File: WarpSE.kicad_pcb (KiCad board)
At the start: 4 copper layers, 112.1 x 102.1 mm, 137 parts, among them J1 MacSEPDS, J2 JTAG, J3 microUSB, J4 DBG, Q1 MMBT3904, Q2 DNP, U1 XC95144XL-TQ100, U10 39SF040, U11 39SF040, U12 CH340G, U13 74AHCT573PW, U14 MC68HC000FN20, U15 74AHCT573PW, U16 74AHCT573PW, U17 74AHCT573PW, U18 74AHCT573PW, U19 74AHCT573PW, U2 74AHCT573PW, U20 74AHCT573PW, U21 74AHCT573PW, U22 74AHCT573PW, U23 74AHCT573PW, U24 74AHCT573PW, U25 LM66100DCK, U26 74LVC1G34GW, U27 74LVC1G34GW, U28 74LVC1G34GW, U29 74LVC1G34GW, U3 AZ1117CH-3.3TRG1, U4 LM66100DCK, U5 50M, U6 74LVC1G74DC, U7 74LVC1G74DC, U8 KM48C2100, U9 KM48C2100, Y1 12M

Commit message: Board changes
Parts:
- removed REF**: PLCC-32_SMDSocket, stdpads:PLCC-32_SMDSocket
- added R38: 1k, stdpads:R_0603, F.Cu at (149.4, 68.7)
- added R39: 1k, stdpads:R_0603, F.Cu at (147.8, 68.7)
- J4: footprint stdpads:PinSocket_2x06_P2.54mm_Vertical -> stdpads:PinSocket_2x06_P2.00mm_Vertical
- U5: value 50M -> SiT2001; footprint stdpads:Crystal_SMD_3225-4Pin_3.2x2.5mm -> stdpads:SOT-23-5
- moved C53 4.41 mm to (125.6, 87.4), turned to -90 degrees
- moved J4 3.33 mm to (105.1, 116.6)
- moved C22 3.28 mm to (103.8, 114.4)
- moved R5 2.06 mm to (132.4, 90.7), turned to 90 degrees
- moved U5 1.65 mm to (128.6, 87.6), turned to 90 degrees
- moved R3 1.15 mm to (127.6, 90.1)
- moved C11 0.85 mm to (122.5, 59.0)
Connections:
- J1 pad C5: /Control/Mac~{BG} -> /PDS/~{BG}
- U1 pad 63: /Control/RA11 -> /Control/BA19
- U1 pad 73: /Control/Mac~{BG} -> /Control/BA18
- U10 pad 28: /Control/RA8 -> /Control/BA18
- U10 pad 29: /Control/RA11 -> /Control/BA19
- U11 pad 25: /Control/RA11 -> /Control/BA19
- U11 pad 26: /Control/RA8 -> /Control/BA18
- U5 pad 1: CLKEN -> GND
- U5 pad 2: GND -> unconnected-(U5-NC-Pad2)
- U5 pad 3: Net-(U5-Output) -> CLKEN
- U8 pad 8: /Control/RA11 -> unconnected-(U8-A11/NC-Pad8)
- U9 pad 10: /Control/RA1 -> /Control/RA2
- U9 pad 11: /Control/RA0 -> /Control/RA1
- U9 pad 12: /Control/RA10 -> /Control/RA0
- U9 pad 13: /Control/RA11 -> /Control/RA3
- U9 pad 8: /Control/RA3 -> unconnected-(U9-A11/NC-Pad8)
- U9 pad 9: /Control/RA2 -> /Control/RA10
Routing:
- net /Control/BA19: track 0.00 -> 173.6 mm, vias 0 -> 6
- net /Control/RA11: track 169.8 -> 0.00 mm, vias 6 -> 0
- net /Control/BA18: track 0.00 -> 153.7 mm, vias 0 -> 7
- net /Control/Mac~{BG}: track 103.4 -> 0.00 mm, vias 3 -> 0
- net /Control/RA8: track 153.2 -> 109.9 mm, vias 6 -> 2
- net /Control/RA3: track 115.6 -> 121.8 mm
- net /Control/DBG1_RAMWS: track 34.7 -> 40.1 mm, vias 1 -> 2
- net /Control/RA10: track 111.2 -> 115.8 mm
- net /Control/CLKINu: track 11.3 -> 14.4 mm
- net /Control/DBG0_ROMWS: track 36.3 -> 38.8 mm, vias 2 -> 1
- net +3V3: track 562.9 -> 565.1 mm, vias 93 -> 92
- net /Buf/GA20: track 107.5 -> 105.4 mm, vias 6 -> 5
- net /Buf/GA21: track 93.2 -> 94.5 mm, vias 5 -> 4
- net CLKEN: track 159.0 -> 158.1 mm
- net Net-(U6-CK): track 8.03 -> 8.90 mm
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
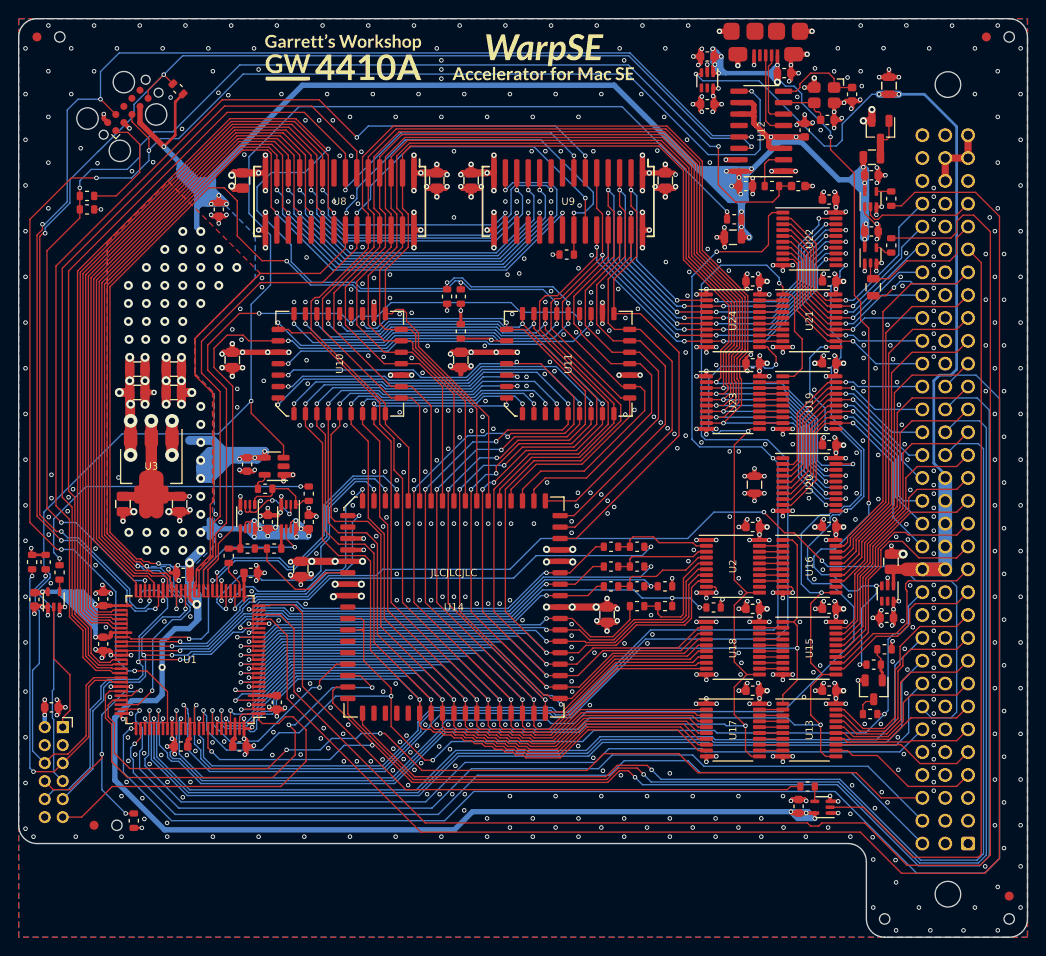
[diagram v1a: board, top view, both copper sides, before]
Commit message: Before remove first clock input buffer
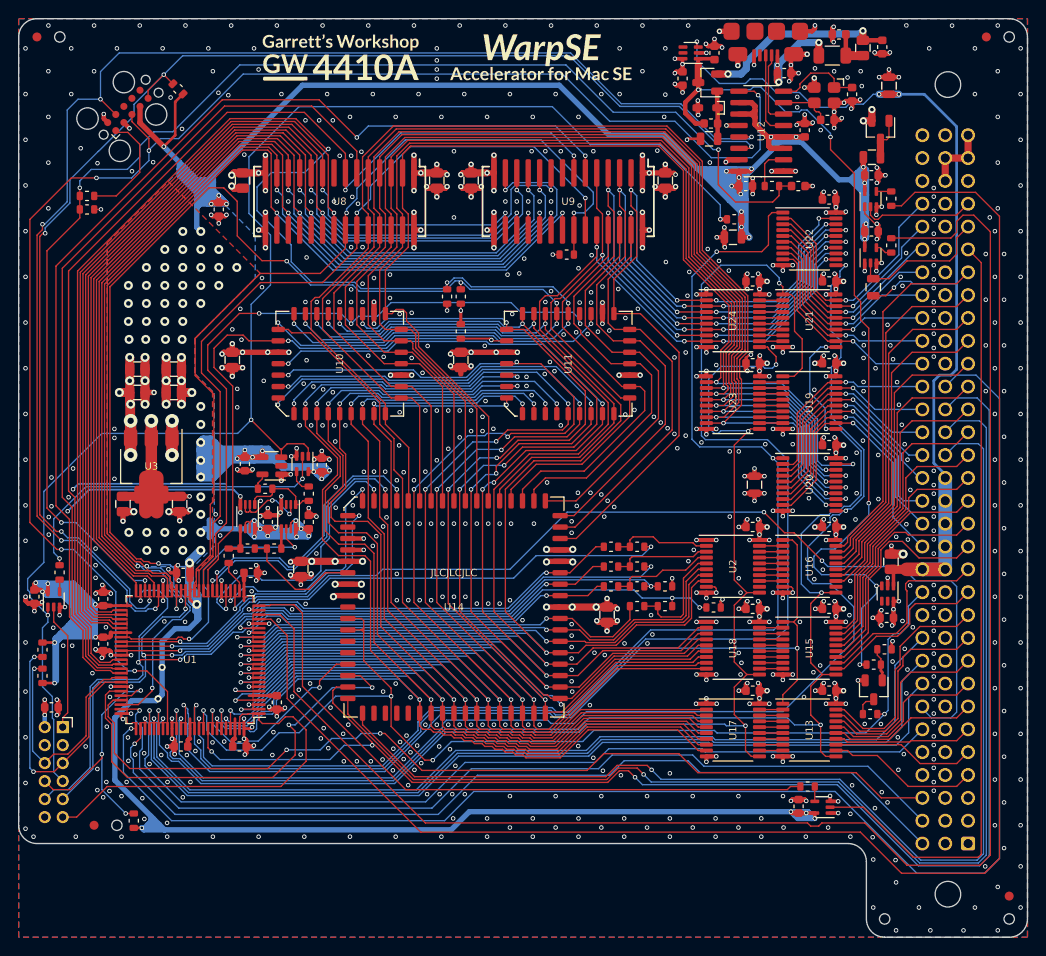
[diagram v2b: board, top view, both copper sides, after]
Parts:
- added C24: 2u2, stdpads:C_0603, F.Cu at (177.2, 49.5)
- added C51: 2u2, stdpads:C_0603, F.Cu at (191.4, 39.6)
- added C55: 2u2, stdpads:C_0603, F.Cu at (196.2, 41.0)
- added C56: 2u2, stdpads:C_0603, F.Cu at (133.9, 87.5)
- added D1: 7V5, stdpads:D_SOD-323, F.Cu at (176.8, 47.8)
- added F1: 750m, stdpads:BelFuse_1206, F.Cu at (190.7, 42.0)
- added FB1: 220, stdpads:C_0805, F.Cu at (194.1, 41.1)
- added Q3: AO3401A, stdpads:SOT-23, F.Cu at (176.8, 45.0)
- added R40: 680, stdpads:R_0805, F.Cu at (176.9, 51.2)
- added U30: 74LVC1G125GW, stdpads:SOT-353, F.Cu at (131.8, 87.3)
- R10, R11, R30, R31, R32, R33, R34, R35, R36, R38, R39, R8: value 1k -> 3k3
- U26, U27, U28, U29: value 74LVC1G34GW -> 74LVC1G32GW
- moved R32 12.7 mm to (102.8, 110.9), turned to -90 degrees
- moved R33 9.81 mm to (102.8, 108.0)
- moved C45 3.96 mm to (174.0, 44.5), turned to -90 degrees
- moved U4 3.57 mm to (174.9, 41.6), turned to 180 degrees
- moved C50 0.89 mm to (177.6, 41.6), turned to 90 degrees
- moved C23 0.30 mm to (102.0, 102.1)
- moved G*** 0.28 mm to (158.3, 42.0)
- moved G*** 0.28 mm to (136.0, 42.4)
- moved C53 0.25 mm to (125.3, 87.3)
- moved U5 0.25 mm to (128.3, 87.5)
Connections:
- C25 pad 1: USB5V -> /Prog/USB5Vf
- J3 pad 1: USB5V -> /Prog/USB5Vf
- R32 pad 2: +5V -> +3V3
- R33 pad 2: +5V -> +3V3
- R34 pad 2: +5V -> +3V3
- R5 pad 2: CLKIN -> Net-(U30-Y)
- U29 pad 1: GND -> CLKEN
- U8 pad 8: unconnected-(U8-A11/NC-Pad8) -> GND
- U9 pad 8: unconnected-(U9-A11/NC-Pad8) -> GND
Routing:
- net +3V3: track 565.1 -> 693.7 mm, vias 92 -> 104
- net GND: track 287.4 -> 336.6 mm, vias 855 -> 883
- net /Prog/USB5Vi: track 0.00 -> 21.8 mm, vias 0 -> 2
- net /Prog/USB5Vf: track 0.00 -> 14.1 mm, vias 0 -> 3
- net USB5V: track 112.6 -> 100.3 mm, vias 10 -> 5
- net /Control/DBG0_ROMWS: track 38.8 -> 27.0 mm
- net /Control/DBG1_RAMWS: track 40.1 -> 30.4 mm
- net CLKEN: track 158.1 -> 165.2 mm, vias 2 -> 3
- net Net-(D1-K): track 0.00 -> 5.32 mm
- net Net-(C51-Pad1): track 0.00 -> 4.25 mm
- net +5V: track 167.9 -> 163.7 mm, vias 119 -> 116
- net Net-(U30-Y): track 0.00 -> 2.65 mm
- net CLKIN: track 35.3 -> 37.4 mm
- net /Buf/AccA1: track 135.1 -> 136.7 mm
- net +5Vin: track 112.2 -> 110.6 mm
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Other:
- board text added: "A10"
